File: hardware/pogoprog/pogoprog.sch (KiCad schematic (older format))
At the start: 12 parts, among them J1 USB-MINI-B, P1 CONN_6, U1 FT232RL

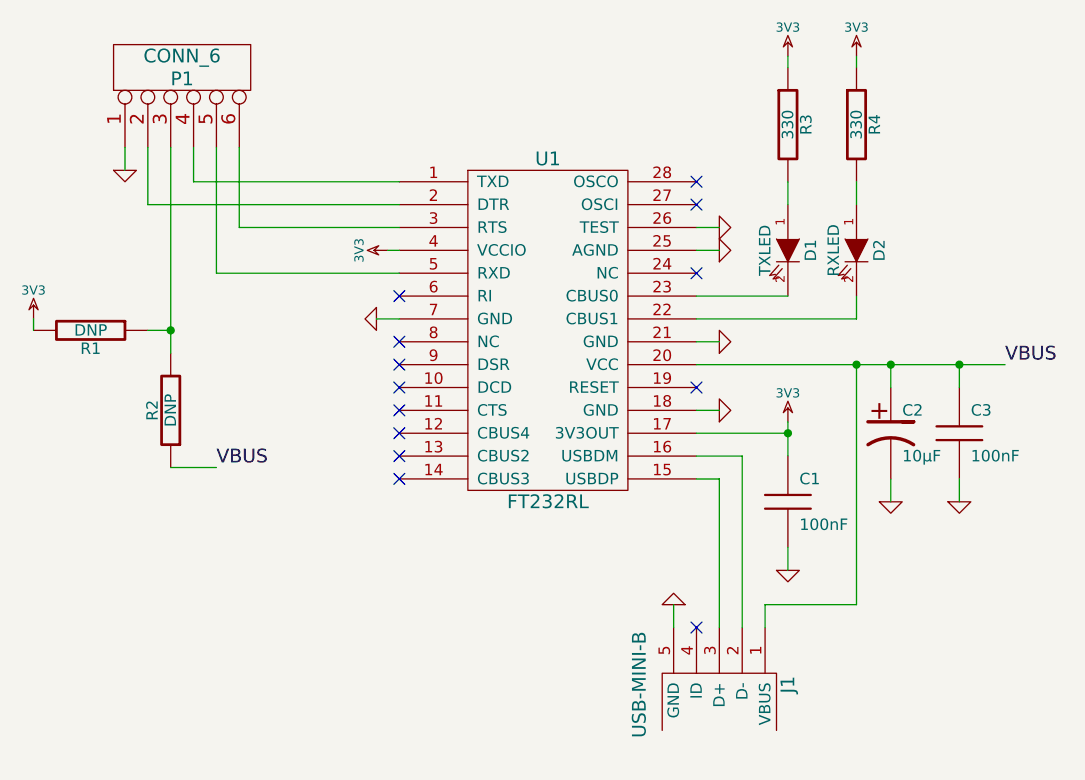
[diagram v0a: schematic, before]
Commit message: labeled some nets
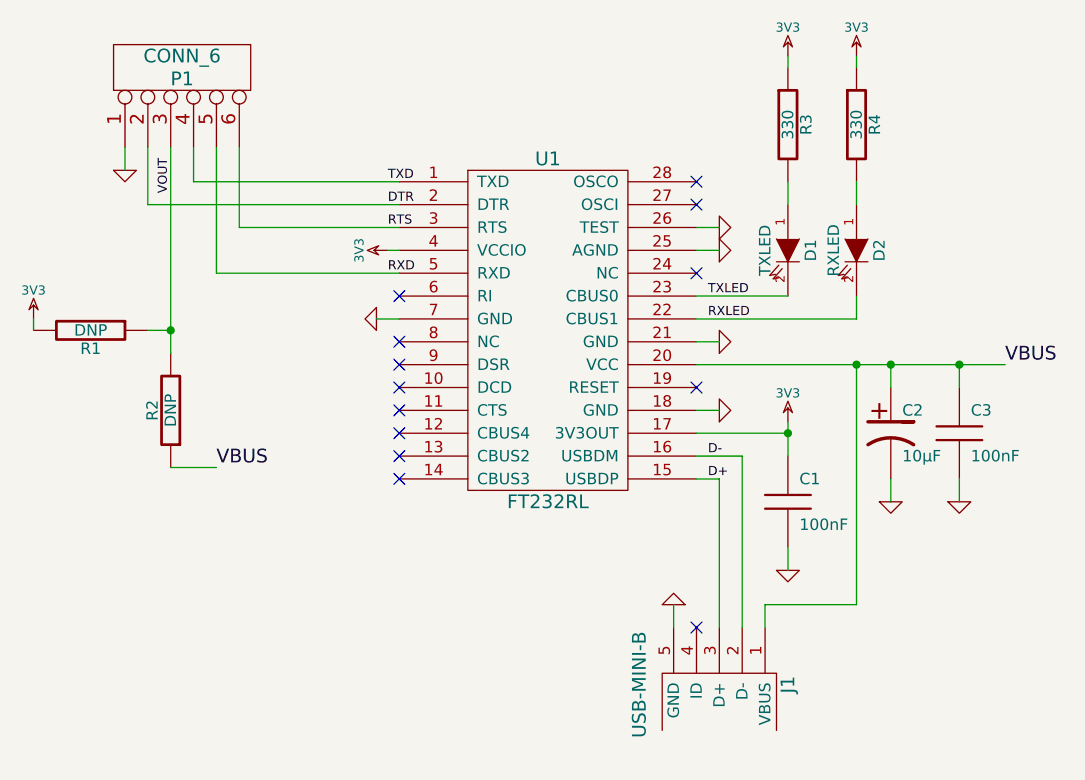
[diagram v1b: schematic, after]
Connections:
- net TXD: now reaches P1.4, U1.1 (TXD)
- net D+: now reaches J1.3 (D+), U1.15 (USBDP)
- net D-: now reaches J1.2 (D-), U1.16 (USBDM)
- net DTR: now reaches P1.2, U1.2 (DTR)
- net RXLED: now reaches D2.2 (K), U1.22 (CBUS1)
- net TXLED: now reaches D1.2 (K), U1.23 (CBUS0)
- net RTS: now reaches P1.6, U1.3 (RTS)
- net RXD: now reaches P1.5, U1.5 (RXD)
- net VOUT: now reaches P1.3, R1.1, R2.2
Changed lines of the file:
@@
-EESchema Schematic File Version 2  date Fri Nov 12 21:16:20 2010
+EESchema Schematic File Version 2  date Sat Nov 13 09:45:15 2010
 LIBS:ubertooth-symbols
 LIBS:power
@@
 Sheet 1 1
 Title "Ubertooth Pogoprog"
-Date "12 nov 2010"
+Date "13 nov 2010"
 Rev "$Rev$"
 Comp "Copyright 2010 Michael Ossmann"
@@
 Comment4 ""
 $EndDescr
+Text Label 4100 3250 1    40   ~ 0
+VOUT
+Text Label 6450 4500 0    40   ~ 0
+D+
+Text Label 6450 4400 0    40   ~ 0
+D-
+Text Label 6450 3800 0    40   ~ 0
+RXLED
+Text Label 6450 3700 0    40   ~ 0
+TXLED
+Text Label 5050 3600 0    40   ~ 0
+RXD
+Text Label 5050 3400 0    40   ~ 0
+RTS
+Text Label 5050 3300 0    40   ~ 0
+DTR
+Text Label 5050 3200 0    40   ~ 0
+TXD
 NoConn ~ 6400 5150
 $Comp
